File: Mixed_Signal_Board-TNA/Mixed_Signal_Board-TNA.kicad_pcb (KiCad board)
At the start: 4 copper layers, 109 parts, among them J200 USB_C_Receptacle_USB2.0_14P, J201 2x5 1.27mm, J300 031-5640-1010, J400 031-5640-1010, U100 HT7533, U102 TLV62569DBV, U2 MCP6001T-E/OT, U200 STM32F103CBT6, U201 USBLC6-2SC6, U300 MCP6001T-E/OT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

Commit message: Done Layout
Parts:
- added C106: DNP, Capacitor_SMD:C_0402_1005Metric, F.Cu at (145.0, 58.5)
- added H1: MountingHole, MountingHole:MountingHole_3.2mm_M3, F.Cu at (97.8, 120.2)
- added H2: MountingHole, MountingHole:MountingHole_3.2mm_M3, F.Cu at (157.2, 120.5)
- added H3: MountingHole, MountingHole:MountingHole_3.2mm_M3, F.Cu at (97.8, 48.8)
- added H4: MountingHole, MountingHole:MountingHole_3.2mm_M3, F.Cu at (157.0, 48.8)
- moved R301 116.3 mm to (105.2, 101.7), turned to 90 degrees
- moved R300 113.2 mm to (107.0, 101.5), turned to -90 degrees
- moved R302 109.9 mm to (110.5, 98.2), turned to 90 degrees
- moved U302 106.3 mm to (111.7, 86.5), turned to 180 degrees
- moved C310 105.1 mm to (114.8, 84.7), turned to 90 degrees
- moved C312 104.3 mm to (114.8, 81.2), turned to -90 degrees
- moved R303 102.6 mm to (116.0, 96.2), turned to -90 degrees
- moved D300 102.2 mm to (112.1, 107.0), turned to 180 degrees
- moved R305 102.1 mm to (114.5, 91.2), turned to -90 degrees
- moved R308 102.1 mm to (113.0, 76.5), turned to 90 degrees
- moved C315 101.4 mm to (117.2, 77.2), turned to 180 degrees
- moved R304 100.9 mm to (116.7, 94.5)
- moved J300 98.8 mm to (110.8, 111.0), turned to 180 degrees
- moved R307 98.4 mm to (117.2, 88.3), turned to -90 degrees
- moved R306 96.1 mm to (119.9, 89.6), turned to -90 degrees
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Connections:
- net Net-(D200-BK) renamed /MCU/B
- net Net-(D200-GK) renamed /MCU/G
- net Net-(D200-RK) renamed /MCU/R
- net Net-(D202-K1) renamed /MCU/CONN_SWDIO
- net Net-(D203-K1) renamed /MCU/CONN_SWCLK
- net Net-(D204-K1) renamed /MCU/CONN_SWO
- net Net-(D205-K1) renamed /MCU/CONN_NRST
- C200 pad 2: <NO NET> -> VREF_DAC
- C201 pad 2: <NO NET> -> VREF_DAC
- C202 pad 2: <NO NET> -> VREF_DAC
- C203 pad 2: <NO NET> -> VREF_DAC
- C204 pad 2: <NO NET> -> VREF_DAC
- C205 pad 2: <NO NET> -> VREF_DAC
- C206 pad 2: <NO NET> -> VREF_DAC
- C207 pad 2: <NO NET> -> VREF_DAC
- C208 pad 2: <NO NET> -> VREF_DAC
- C209 pad 2: <NO NET> -> VREF_DAC
- C210 pad 2: <NO NET> -> VREF_DAC
- C211 pad 1: <NO NET> -> VREF_DAC
- C212 pad 1: <NO NET> -> VREF_DAC
- D201 pad 2: <NO NET> -> VREF_DAC
- D202 pad 2: <NO NET> -> VREF_DAC
- D203 pad 2: <NO NET> -> VREF_DAC
- D204 pad 2: <NO NET> -> VREF_DAC
- D205 pad 2: <NO NET> -> VREF_DAC
- J200 pad A1: <NO NET> -> VREF_DAC
- J200 pad A12: <NO NET> -> VREF_DAC
- J200 pad B1: <NO NET> -> VREF_DAC
- J200 pad B12: <NO NET> -> VREF_DAC
- J201 pad 3: <NO NET> -> VREF_DAC
- J201 pad 5: <NO NET> -> VREF_DAC
- J201 pad 9: <NO NET> -> VREF_DAC
- R200 pad 1: <NO NET> -> VREF_DAC
- R205 pad 1: <NO NET> -> VREF_DAC
- R206 pad 1: <NO NET> -> VREF_DAC
- U200 pad 23: <NO NET> -> VREF_DAC
- U200 pad 35: <NO NET> -> VREF_DAC
- U200 pad 47: <NO NET> -> VREF_DAC
- U200 pad 8: <NO NET> -> VREF_DAC
- U201 pad 2: <NO NET> -> VREF_DAC
- Y200 pad 2: <NO NET> -> VREF_DAC
- Y200 pad 4: <NO NET> -> VREF_DAC
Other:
- board outline added: 69.3 x 81.5 mm

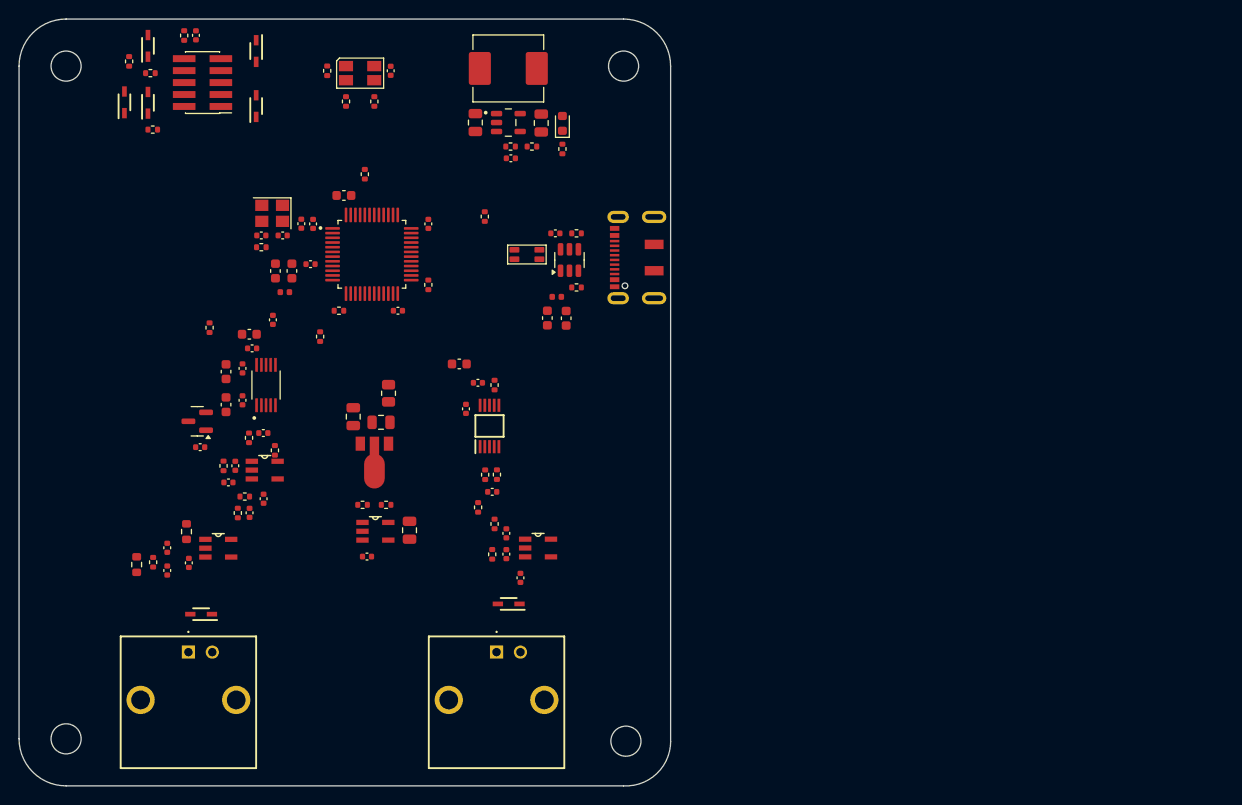
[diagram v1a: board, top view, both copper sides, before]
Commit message: Routed but differential pair not right
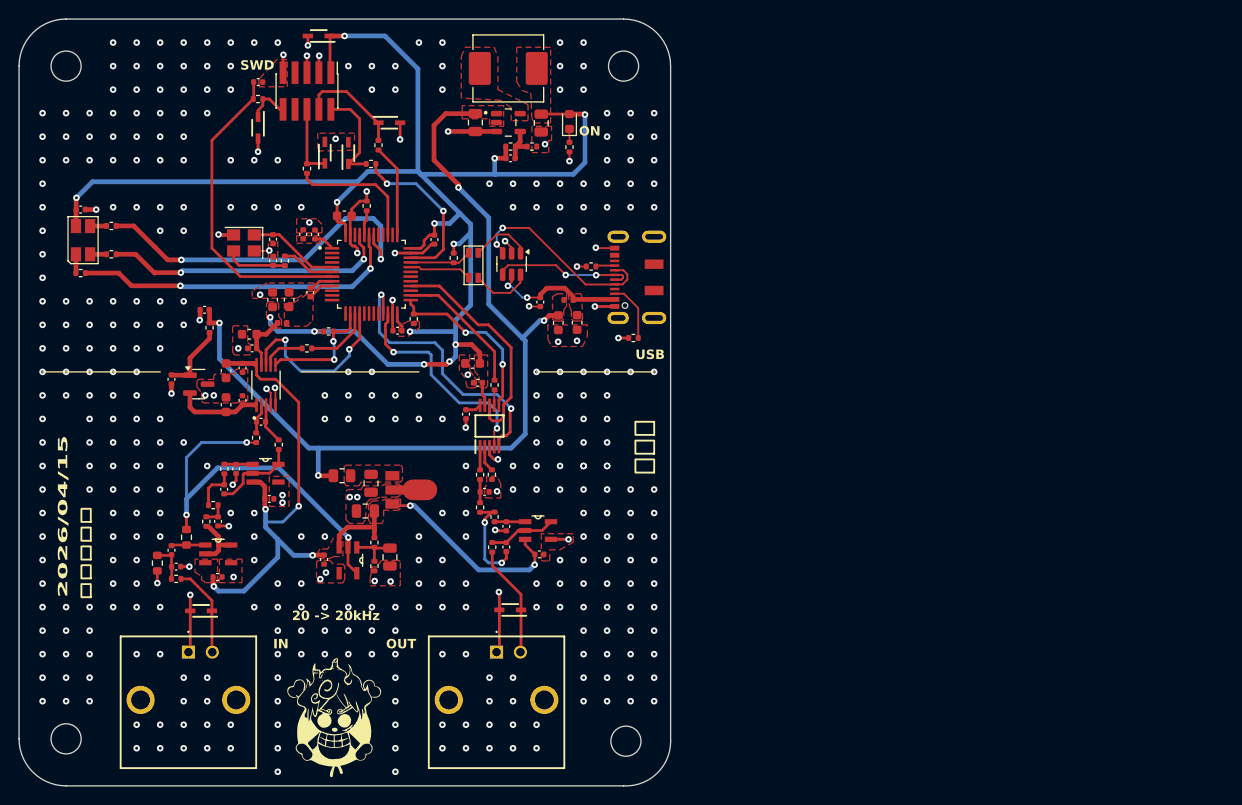
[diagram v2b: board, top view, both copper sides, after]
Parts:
- added G***: LOGO, LOGO, F.Cu at (126.2, 118.0)
- moved C210 36.1 mm to (99.3, 64.0), turned to 0 degrees
- moved D200 34.4 mm to (99.5, 67.2), turned to 90 degrees
- moved R208 33.9 mm to (99.3, 70.8), turned to 180 degrees
- moved R207 30.9 mm to (102.6, 65.7), turned to 180 degrees
- moved R209 29.8 mm to (102.6, 68.8), turned to 180 degrees
- moved R211 28.0 mm to (130.9, 57.2)
- moved D203 26.9 mm to (132.1, 54.8), turned to 0 degrees
- moved R210 23.5 mm to (130.2, 59.1)
- moved D202 22.0 mm to (127.8, 58.0)
- moved D204 22.0 mm to (125.2, 58.0)
- moved R212 19.5 mm to (123.3, 59.6), turned to 90 degrees
- moved J201 11.1 mm to (123.3, 51.4), turned to -90 degrees
- moved R213 10.4 mm to (118.2, 52.2), turned to 0 degrees
- moved C103 10.1 mm to (129.6, 96.0), turned to 180 degrees
- moved R100 10.1 mm to (127.1, 92.3), turned to 0 degrees
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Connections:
- net Net-(U200-BOOT0) renamed /MCU/BOOT0
- C105 pad 1: +3.3V -> +3V3
- C106 pad 1: +3.3V -> +3V3
- D100 pad 2: +3.3V -> +3V3
- L101 pad 2: +3.3V -> +3V3
- R101 pad 1: +3.3V -> +3V3
- U201 pad 4: /MCU/USB_CONN_D- -> /MCU/USB_CONN_D+
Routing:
- net +3V3: track 0.00 -> 185.1 mm, vias 0 -> 13
- net +5V: track 0.00 -> 94.4 mm, vias 0 -> 4
- net +3.3VA: track 0.00 -> 79.8 mm, vias 0 -> 6
- net VREF_DAC: track 0.00 -> 77.7 mm, vias 0 -> 409
- net VCOM: track 0.00 -> 43.3 mm, vias 0 -> 3
- net /MCU/TIM4_CH1: track 0.00 -> 38.2 mm, vias 0 -> 2
- net /MCU/TIM4_CH2: track 0.00 -> 35.3 mm, vias 0 -> 2
- net /MCU/NRST: track 0.00 -> 33.6 mm
- net /MCU/TIM4_CH3: track 0.00 -> 30.5 mm, vias 0 -> 2
- net DAC_NCLR: track 0.00 -> 29.9 mm, vias 0 -> 2
- net SPI2_MOSI: track 0.00 -> 24.2 mm
- net DAC_NLDAC: track 0.00 -> 23.3 mm, vias 0 -> 2
- net /MCU/USB_CONN_D-: track 0.00 -> 21.2 mm, vias 0 -> 2
- net SPI1_MISO: track 0.00 -> 18.9 mm, vias 0 -> 2
- net SPI2_NSS: track 0.00 -> 18.8 mm, vias 0 -> 2
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- added copper zone on F.Cu, net +3.3VA
- added copper zone on F.Cu, net +3V3
- added copper zone on F.Cu, net +5V
- added copper zone on F.Cu, net /Power/+5V_FILT
- added copper zone on F.Cu, net /Power/BUCK_SW
- added copper zone on F.Cu, net VBUS
- added copper zone on F.Cu, net VDDA
- added copper zone on F.Cu, net VREF_DAC
- added copper zone on In1.Cu, net VREF_DAC
- added copper zone on In2.Cu, net VREF_DAC
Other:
- board text added: "1 MOhm"
- board text added: "20 -> 20kHz"
- board text added: "2026/04/15"
- board text added: "50 Ohm"
- board text added: "IN"
- board text added: "ON"
- board text added: "OUT"
- board text added: "S"
- board text added: "SWD"
- board text added: "USB"
- board text added: "朱天佑"
- board text added: "ＲＥＶ １"
